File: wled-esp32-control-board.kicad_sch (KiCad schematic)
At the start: 6 parts, among them J101 Barrel_Jack_MountingPin, U101 ESP32-WROOM-32

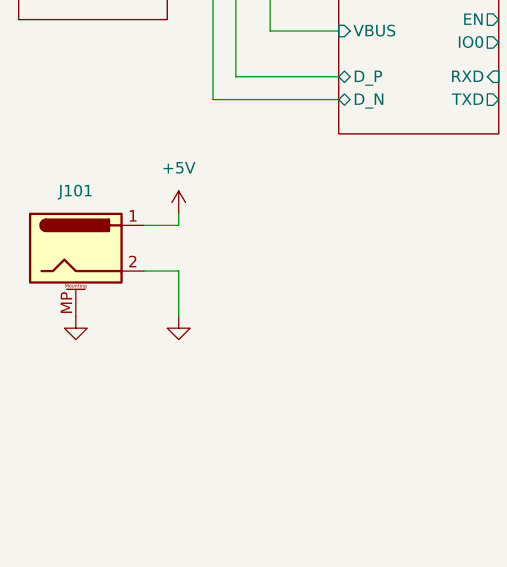
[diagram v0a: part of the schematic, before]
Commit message: update barrel jack
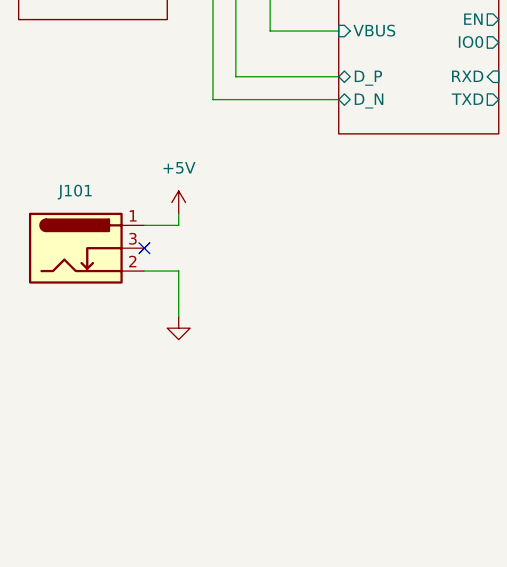
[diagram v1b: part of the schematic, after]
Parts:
- J101: footprint Connector_BarrelJack:BarrelJack_CUI_PJ-063AH_Horizontal -> Connector_BarrelJack:BarrelJack_Horizontal; symbol Connector:Barrel_Jack_MountingPin -> Connector:Barrel_Jack_Switch; LCSC (none) -> C381115
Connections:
- net GND: no longer J101.MP (MountPin)
- no-connect marks 27 -> 28
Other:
- moved on the sheet: J101
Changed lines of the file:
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@@
   (no_connect (at 234.95 72.39))
   (no_connect (at 234.95 82.55))
+  (no_connect (at 36.83 76.2))
   (no_connect (at 234.95 64.77))
   (no_connect (at 234.95 90.17))
@@
         (path "/39949f26-7b4e-4f4c-975a-4ef261468b2a"
           (reference "#PWR0103") (unit 1)
-        )
-      )
-    )
-  )
-  (symbol (lib_id "power:GND") (at 29.21 83.82 0) (unit 1)
-    (in_bom yes) (on_board yes) (dnp no) (fields_autoplaced)
-    (property "Reference" "#PWR0102" (at 29.21 90.17 0)
-      (effects (font (size 1.27 1.27)) hide)
-    )
-    (property "Value" "GND" (at 29.21 88.9 0)
-      (effects (font (size 1.27 1.27)) hide)
-    )
-    (property "Footprint" "" (at 29.21 83.82 0)
-      (effects (font (size 1.27 1.27)) hide)
-    )
-    (property "Datasheet" "" (at 29.21 83.82 0)
-      (effects (font (size 1.27 1.27)) hide)
-    )
-    (pin "1")
-    (instances
-      (project "wled-esp32-control-board"
-        (path "/39949f26-7b4e-4f4c-975a-4ef261468b2a"
-          (reference "#PWR0102") (unit 1)
         )
       )
@@
     )
   )
-  (symbol (lib_id "Connector:Barrel_Jack_MountingPin") (at 29.21 76.2 0) (unit 1)
+  (symbol (lib_id "Connector:Barrel_Jack_Switch") (at 29.21 76.2 0) (unit 1)
     (in_bom yes) (on_board yes) (dnp no) (fields_autoplaced)
     (property "Reference" "J101" (at 29.21 69.85 0)
@@
       (effects (font (size 1.27 1.27)) hide)
     )
-    (property "Footprint" "Connector_BarrelJack:BarrelJack_CUI_PJ-063AH_Horizontal" (at 30.48 77.216 0)
+    (property "Footprint" "Connector_BarrelJack:BarrelJack_Horizontal" (at 30.48 77.216 0)
       (effects (font (size 1.27 1.27)) hide)
     )
@@
       (effects (font (size 1.27 1.27)) hide)
     )
+    (property "LCSC" "C381115" (at 29.21 76.2 0)
+      (effects (font (size 1.27 1.27)) hide)
+    )
+    (property "Mouser" "" (at 29.21 76.2 0)
+      (effects (font (size 1.27 1.27)) hide)
+    )
+    (property "DigiKey" "" (at 29.21 76.2 0)
+      (effects (font (size 1.27 1.27)) hide)
+    )
     (pin "1")
     (pin "2")
-    (pin "MP")
-    (instances
-      (project "wled-esp32-control-board"
+    (pin "3")
+    (instances
+      (project "wled-esp32-control-board"

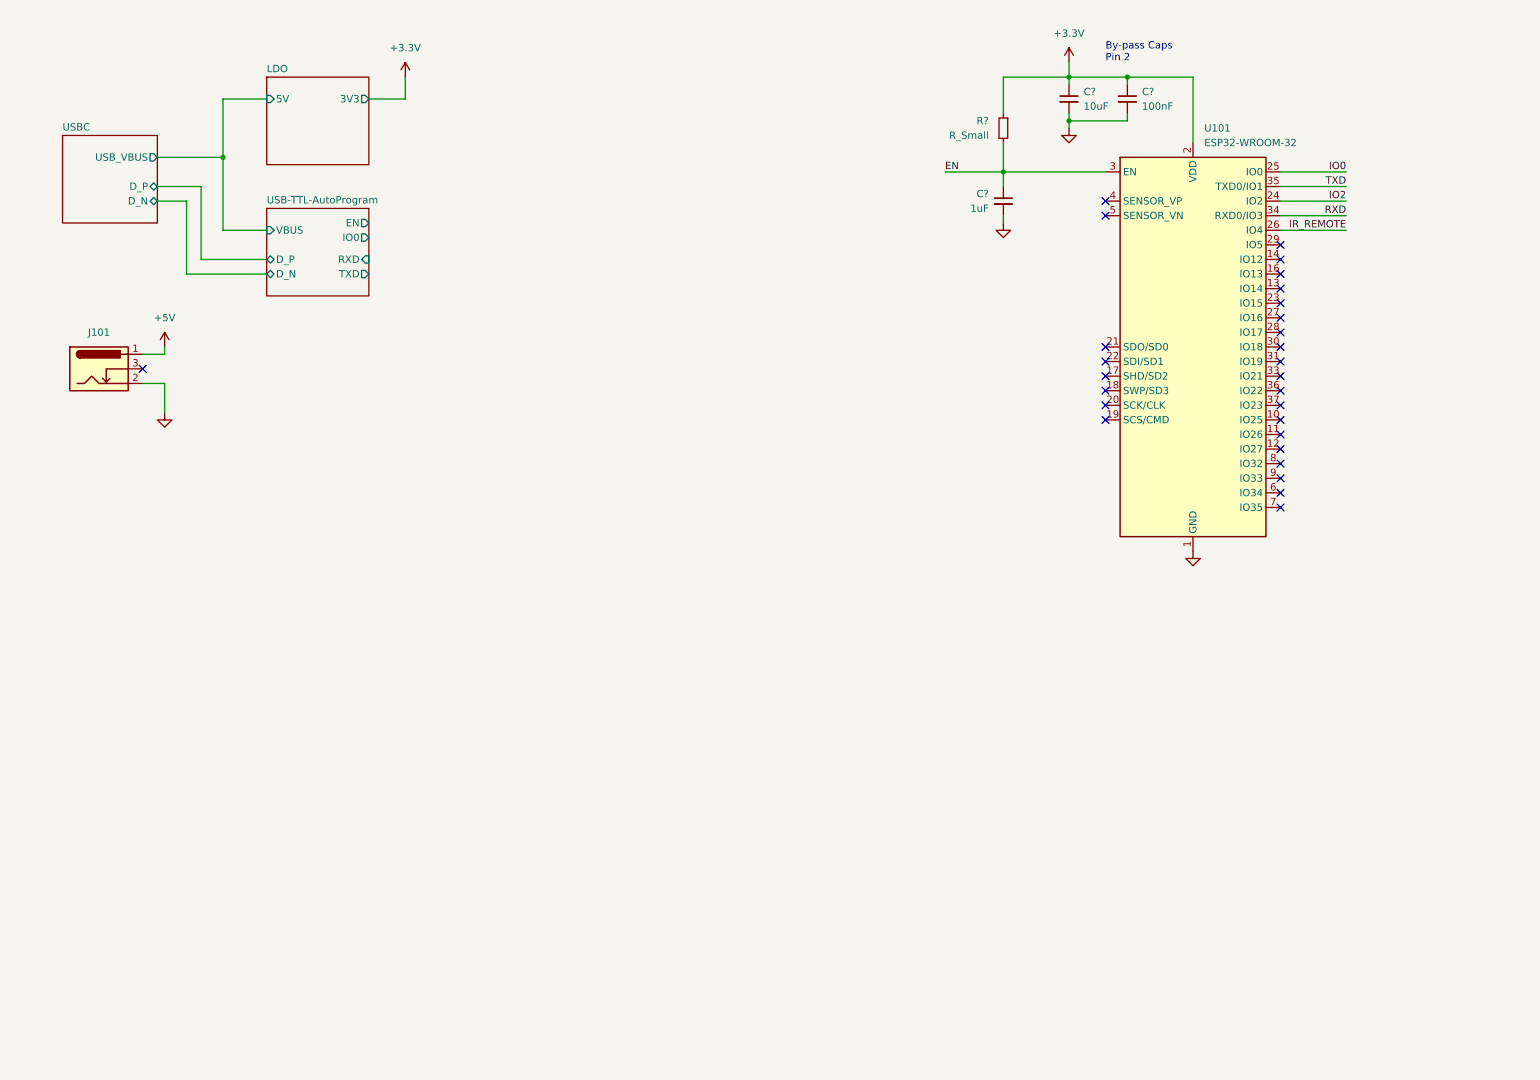
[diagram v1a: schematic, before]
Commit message: update schematic
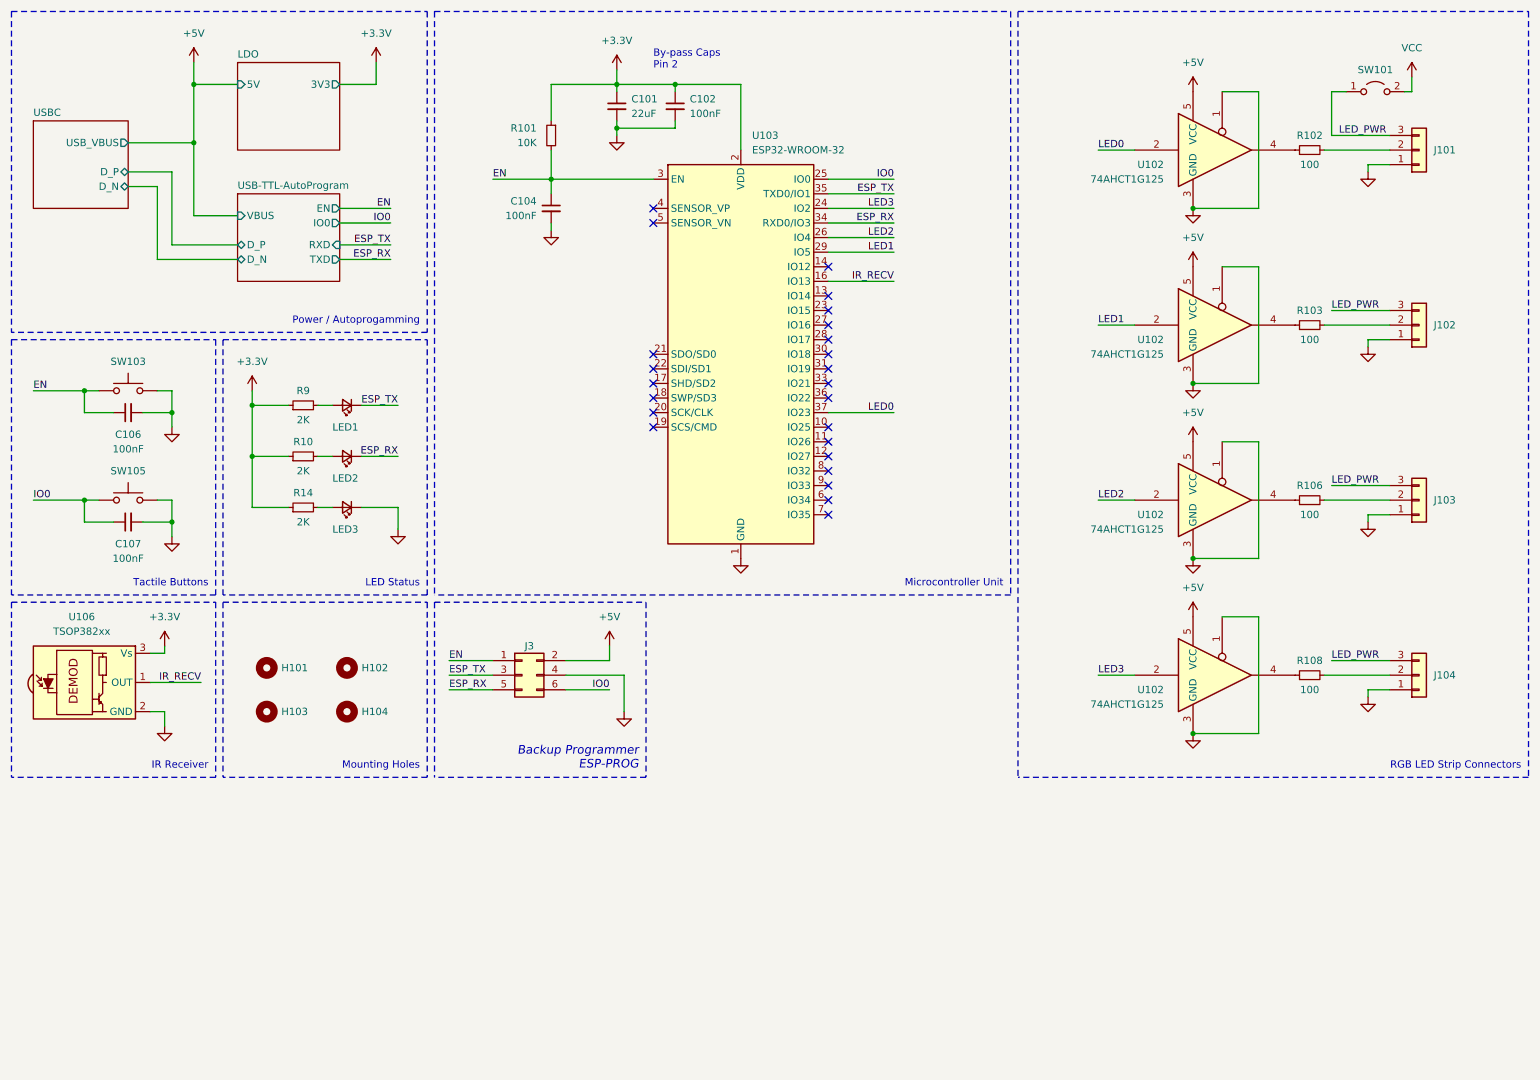
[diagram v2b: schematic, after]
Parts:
- removed J101: Barrel_Jack_MountingPin, Connector_BarrelJack:BarrelJack_Horizontal, symbol Connector:Barrel_Jack_Switch
- added C106, C107: 100nF, Capacitor_SMD:C_0603_1608Metric, symbol Device:C_Small
- added H101, H102, H103, H104: MountingHole, MountingHole:MountingHole_3.2mm_M3, symbol Mechanical:MountingHole
- added J101, J102, J103, J104: Conn_01x03, User_Footprint:molex-39773-0003, symbol Connector_Generic:Conn_01x03
- added J3: Conn_02x03_Odd_Even, Connector_Tag:TC2030-IDC-NL, symbol Connector_Generic:Conn_02x03_Odd_Even
- added LED1: BLUE, LED_SMD:LED_0603_1608Metric, symbol Device:LED_Small
- added LED2: GREEN, LED_SMD:LED_0603_1608Metric, symbol Device:LED_Small
- added LED3: RED, LED_SMD:LED_0603_1608Metric, symbol Device:LED_Small
- added R10, R14, R9: 2K, Resistor_SMD:R_0603_1608Metric, symbol Device:R_Small
- added R102, R103, R106, R108: 100, Resistor_SMD:R_0603_1608Metric, symbol Device:R_Small
- added SW101: SW_SPDT, Connector_PinHeader_2.54mm:PinHeader_1x02_P2.54mm_Vertical, symbol Jumper:Jumper_2_Open
- added SW103, SW105: SW_Push, User_Footprint:XKB-Connectivity-TS-1187A-B-A-B, symbol Switch:SW_Push
- added U102 (x4): 74AHCT1G125, Package_TO_SOT_SMD:SOT-23-5, symbol 74xGxx:74AHCT1G125
- added U106: TSOP382xx, OptoDevice:Vishay_MINICAST-3Pin, symbol Interface_Optical:TSOP382xx
- C101: renamed from C?; value 10uF -> 22uF; footprint (none) -> Capacitor_SMD:C_0603_1608Metric; LCSC (none) -> C59461
- C102: renamed from C?; footprint (none) -> Capacitor_SMD:C_0603_1608Metric; LCSC (none) -> C14663
- C104: renamed from C?; value 1uF -> 100nF; footprint (none) -> Capacitor_SMD:C_0603_1608Metric; LCSC (none) -> C14663
- R101: renamed from R?; value R_Small -> 10K; footprint (none) -> Resistor_SMD:R_0603_1608Metric; LCSC (none) -> C25804
- renumbered U101 to U103
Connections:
- net +3.3V: now also R10.1, R14.1, R9.1, U106.3 (Vs)
- net +5V: now also J3.2 (Pin_2), U102.5 (VCC), U102.5 (VCC), U102.5 (VCC), U102.5 (VCC)
- net EN: now also C106.1, J3.1 (Pin_1), SW103.1
- net GND: now also C106.2, C107.2, J101.1 (Pin_1), J102.1 (Pin_1), J103.1 (Pin_1), J104.1 (Pin_1), J3.4 (Pin_4), LED3.1 (K), SW103.2, SW105.2, U102.1, U102.1, U102.1, U102.1, U102.3 (GND), U102.3 (GND), U102.3 (GND), U102.3 (GND), U106.2 (GND)
- net IO0: now also C107.1, J3.6 (Pin_6), SW105.1
- net IR_RECV: now reaches U103.16 (IO13)
- net IR_RECV: now also U106.1 (OUT)
- net LED1: now reaches U103.29 (IO5)
- net LED1: now also U102.2
- net LED0: now reaches U103.37 (IO23)
- net LED0: now also U102.2
- net IO2 renamed LED3
- net LED3: now also U102.2
- net IR_REMOTE renamed LED2
- net LED2: now also U102.2
- net RXD renamed ESP_RX
- net ESP_RX: now also J3.5 (Pin_5), LED2.1 (K)
- net TXD renamed ESP_TX
- net ESP_TX: now also J3.3 (Pin_3), LED1.1 (K)
- new net: R106.1, U102.4
- new net: J103.2 (Pin_2), R106.2
- new net: R103.1, U102.4
- new net: LED2.2 (A), R10.2
- new net: LED1.2 (A), R9.2
- new net: J102.2 (Pin_2), R103.2
- new net: J104.2 (Pin_2), R108.2
- new net: LED3.2 (A), R14.2
- new net: R108.1, U102.4
- new net: J101.2 (Pin_2), R102.2
- new net: R102.1, U102.4
- new net LED_PWR: J101.3 (Pin_3), J102.3 (Pin_3), J103.3 (Pin_3), J104.3 (Pin_3), SW101.1 (A)
- new net VCC: SW101.2 (B)
- no-connect marks 28 -> 24
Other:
- note added: "Backup Programmer ESP-PROG"
- note added: "IR Receiver"
- note added: "LED Status"
- note added: "Microcontroller Unit"
- note added: "Mounting Holes"
- note added: "Power / Autoprogamming"
- note added: "RGB LED Strip Connectors"
- note added: "Tactile Buttons"
- moved on the sheet: C101, C102, C104, R101, U103

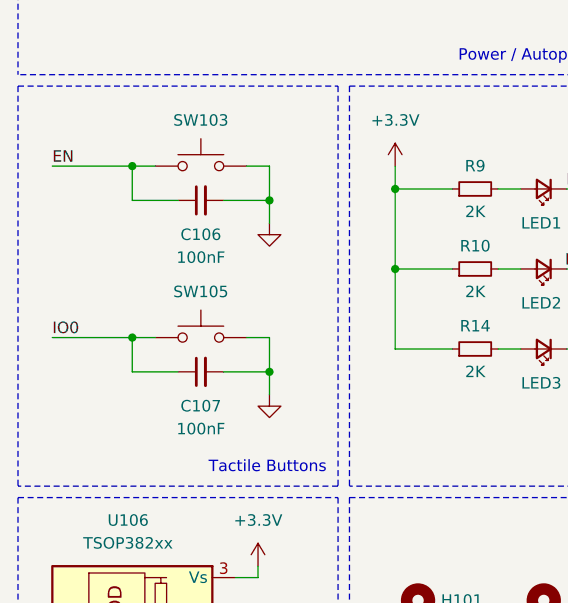
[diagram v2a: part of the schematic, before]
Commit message: remove caps from tactile button
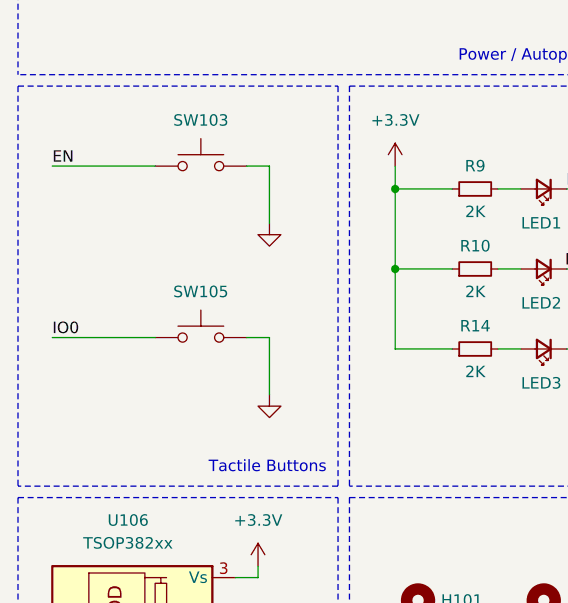
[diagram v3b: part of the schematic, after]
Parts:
- removed C106, C107: 100nF, Capacitor_SMD:C_0603_1608Metric, symbol Device:C_Small
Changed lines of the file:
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@@
   (junction (at 119.38 34.29) (diameter 0) (color 0 0 0 0)
   )
-  (junction (at 41.91 102.87) (diameter 0) (color 0 0 0 0)
-  )
   (junction (at 55.88 82.55) (diameter 0) (color 0 0 0 0)
   )
-  (junction (at 41.91 83.82) (diameter 0) (color 0 0 0 0)
-  )
   (junction (at 219.71 48.26) (diameter 0) (color 0 0 0 0)
   )
   (junction (at 219.71 78.74) (diameter 0) (color 0 0 0 0)
   )
-  (junction (at 26.67 80.01) (diameter 0) (color 0 0 0 0)
-  )
   (junction (at 119.38 26.67) (diameter 0) (color 0 0 0 0)
   )
   (junction (at 129.54 26.67) (diameter 0) (color 0 0 0 0)
-  )
-  (junction (at 26.67 99.06) (diameter 0) (color 0 0 0 0)
   )
   (junction (at 45.72 36.83) (diameter 0) (color 0 0 0 0)
@@
     (stroke (width 0) (type default))
   )
-  (wire (pts (xy 36.83 102.87) (xy 41.91 102.87))
-    (stroke (width 0) (type default))
-  )
   (wire (pts (xy 250.19 132.08) (xy 254 132.08))
     (stroke (width 0) (type default))
@@
     (stroke (width 0) (type default))
   )
-  (wire (pts (xy 41.91 99.06) (xy 41.91 102.87))
+  (wire (pts (xy 41.91 99.06) (xy 41.91 105.41))
     (stroke (width 0) (type default))
   )
@@
     (stroke (width 0) (type default))
   )
-  (wire (pts (xy 26.67 99.06) (xy 29.21 99.06))
+  (wire (pts (xy 17.78 99.06) (xy 29.21 99.06))
     (stroke (width 0) (type default))
   )
@@
     (stroke (width 0) (type default))
   )
-  (wire (pts (xy 41.91 102.87) (xy 41.91 105.41))
-    (stroke (width 0) (type default))
-  )
   (wire (pts (xy 156.21 83.82) (xy 167.64 83.82))
     (stroke (width 0) (type default))
@@
     (stroke (width 0) (type default))
   )
-  (wire (pts (xy 31.75 83.82) (xy 26.67 83.82))
-    (stroke (width 0) (type default))
-  )
   (wire (pts (xy 119.38 26.67) (xy 107.95 26.67))
     (stroke (width 0) (type default))
@@
     (stroke (width 0) (type default))
   )
-  (wire (pts (xy 41.91 83.82) (xy 41.91 86.36))
-    (stroke (width 0) (type default))
-  )
   (wire (pts (xy 250.19 71.12) (xy 250.19 72.39))
     (stroke (width 0) (type default))
@@
     (stroke (width 0) (type default))
   )
-  (wire (pts (xy 36.83 83.82) (xy 41.91 83.82))
-    (stroke (width 0) (type default))
-  )
   (wire (pts (xy 119.38 34.29) (xy 119.38 33.02))
     (stroke (width 0) (type default))
@@
     (stroke (width 0) (type default))
   )
-  (wire (pts (xy 17.78 99.06) (xy 26.67 99.06))
-    (stroke (width 0) (type default))
-  )
   (wire (pts (xy 119.38 24.13) (xy 119.38 26.67))
     (stroke (width 0) (type default))
@@
     (stroke (width 0) (type default))
   )
-  (wire (pts (xy 26.67 102.87) (xy 26.67 99.06))
-    (stroke (width 0) (type default))
-  )
   (polyline (pts (xy 50.8 71.12) (xy 86.36 71.12))
     (stroke (width 0) (type dash))
@@
     (stroke (width 0) (type default))
   )
-  (wire (pts (xy 17.78 80.01) (xy 26.67 80.01))
-    (stroke (width 0) (type default))
-  )
-  (wire (pts (xy 41.91 80.01) (xy 41.91 83.82))
+  (wire (pts (xy 17.78 80.01) (xy 29.21 80.01))
+    (stroke (width 0) (type default))
+  )
+  (wire (pts (xy 41.91 80.01) (xy 41.91 86.36))
     (stroke (width 0) (type default))
   )
@@
     (stroke (width 0) (type default))
   )
-  (wire (pts (xy 31.75 102.87) (xy 26.67 102.87))
-    (stroke (width 0) (type default))
-  )
   (wire (pts (xy 119.38 34.29) (xy 129.54 34.29))
     (stroke (width 0) (type default))
   )
-  (wire (pts (xy 26.67 83.82) (xy 26.67 80.01))
-    (stroke (width 0) (type default))
-  )
   (polyline (pts (xy 13.97 13.97) (xy 86.36 13.97))
     (stroke (width 0) (type dash))
-  )
-  (wire (pts (xy 26.67 80.01) (xy 29.21 80.01))
-    (stroke (width 0) (type default))
   )
   (wire (pts (xy 119.38 26.67) (xy 129.54 26.67))
@@
         (path "/a2f2828e-5f72-4b22-816e-2a917e094849"
           (reference "#PWR0136") (unit 1)
-        )
-      )
-    )
-  )
-  (symbol (lib_id "Device:C_Small") (at 34.29 102.87 90) (unit 1)
-    (in_bom yes) (on_board yes) (dnp no)
-    (property "Reference" "C107" (at 34.29 106.68 90)
-      (effects (font (size 1.27 1.27)))
-    )
-    (property "Value" "100nF" (at 34.29 109.22 90)
-      (effects (font (size 1.27 1.27)))
-    )
-    (property "Footprint" "Capacitor_SMD:C_0603_1608Metric" (at 34.29 102.87 0)
-      (effects (font (size 1.27 1.27)) hide)
-    )
-    (property "Datasheet" "~" (at 34.29 102.87 0)
-      (effects (font (size 1.27 1.27)) hide)
-    )
-    (property "LCSC" "C14663" (at 34.29 102.87 0)
-      (effects (font (size 1.27 1.27)) hide)
-    )
-    (pin "1")
-    (pin "2")
-    (instances
-      (project "wled-esp32-control-board"
-        (path "/39949f26-7b4e-4f4c-975a-4ef261468b2a"
-          (reference "C107") (unit 1)
-        )
-      )
-      (project "7-segment-display-controller"
-        (path "/a2f2828e-5f72-4b22-816e-2a917e094849"
-          (reference "C114") (unit 1)
         )
       )
@@
         )
       )
-    )
-  )
-  (symbol (lib_id "Device:C_Small") (at 34.29 83.82 90) (unit 1)
-    (in_bom yes) (on_board yes) (dnp no)
-    (property "Reference" "C106" (at 34.29 87.63 90)
-      (effects (font (size 1.27 1.27)))
-    )
-    (property "Value" "100nF" (at 34.29 90.17 90)
-      (effects (font (size 1.27 1.27)))
-    )
-    (property "Footprint" "Capacitor_SMD:C_0603_1608Metric" (at 34.29 83.82 0)
-      (effects (font (size 1.27 1.27)) hide)
-    )
-    (property "Datasheet" "~" (at 34.29 83.82 0)
-      (effects (font (size 1.27 1.27)) hide)
-    )
-    (property "LCSC" "C14663" (at 34.29 83.82 0)
-      (effects (font (size 1.27 1.27)) hide)
-    )
-    (pin "1")
-    (pin "2")
-    (instances
-      (project "wled-esp32-control-board"
-        (path "/39949f26-7b4e-4f4c-975a-4ef261468b2a"
-          (reference "C106") (unit 1)
-        )
-      )
-      (project "7-segment-display-controller"
-        (path "/a2f2828e-5f72-4b22-816e-2a917e094849"
-          (reference "C114") (unit 1)
-        )
-      )

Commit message: update BOM status
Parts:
- SW101, U106: now left out of the parts list
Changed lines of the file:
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@@
   )
   (symbol (lib_id "Interface_Optical:TSOP382xx") (at 27.94 130.81 0) (unit 1)
-    (in_bom yes) (on_board yes) (dnp no) (fields_autoplaced)
+    (in_bom no) (on_board yes) (dnp no) (fields_autoplaced)
     (property "Reference" "U106" (at 26.205 119.38 0)
       (effects (font (size 1.27 1.27)))
@@
     )
     (property "Mouser" "782-TSOP38238" (at 27.94 130.81 0)
+      (effects (font (size 1.27 1.27)) hide)
+    )
+    (property "LCSC" "" (at 27.94 130.81 0)
       (effects (font (size 1.27 1.27)) hide)
     )
@@
   )
   (symbol (lib_id "Jumper:Jumper_2_Open") (at 251.46 27.94 0) (unit 1)
-    (in_bom yes) (on_board yes) (dnp no) (fields_autoplaced)
+    (in_bom no) (on_board yes) (dnp no) (fields_autoplaced)
     (property "Reference" "SW101" (at 251.46 24.13 0)
       (effects (font (size 1.27 1.27)))
@@
       (effects (font (size 1.27 1.27)) hide)
     )
+    (property "LCSC" "" (at 251.46 27.94 0)
+      (effects (font (size 1.27 1.27)) hide)
+    )
